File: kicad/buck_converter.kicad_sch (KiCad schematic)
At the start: 51 parts, among them J1 XT30U-M, J2 XT30U-F, Q1 BSZ146N10LS5ATMA1, Q2 BSZ146N10LS5ATMA1, U1 LM5146

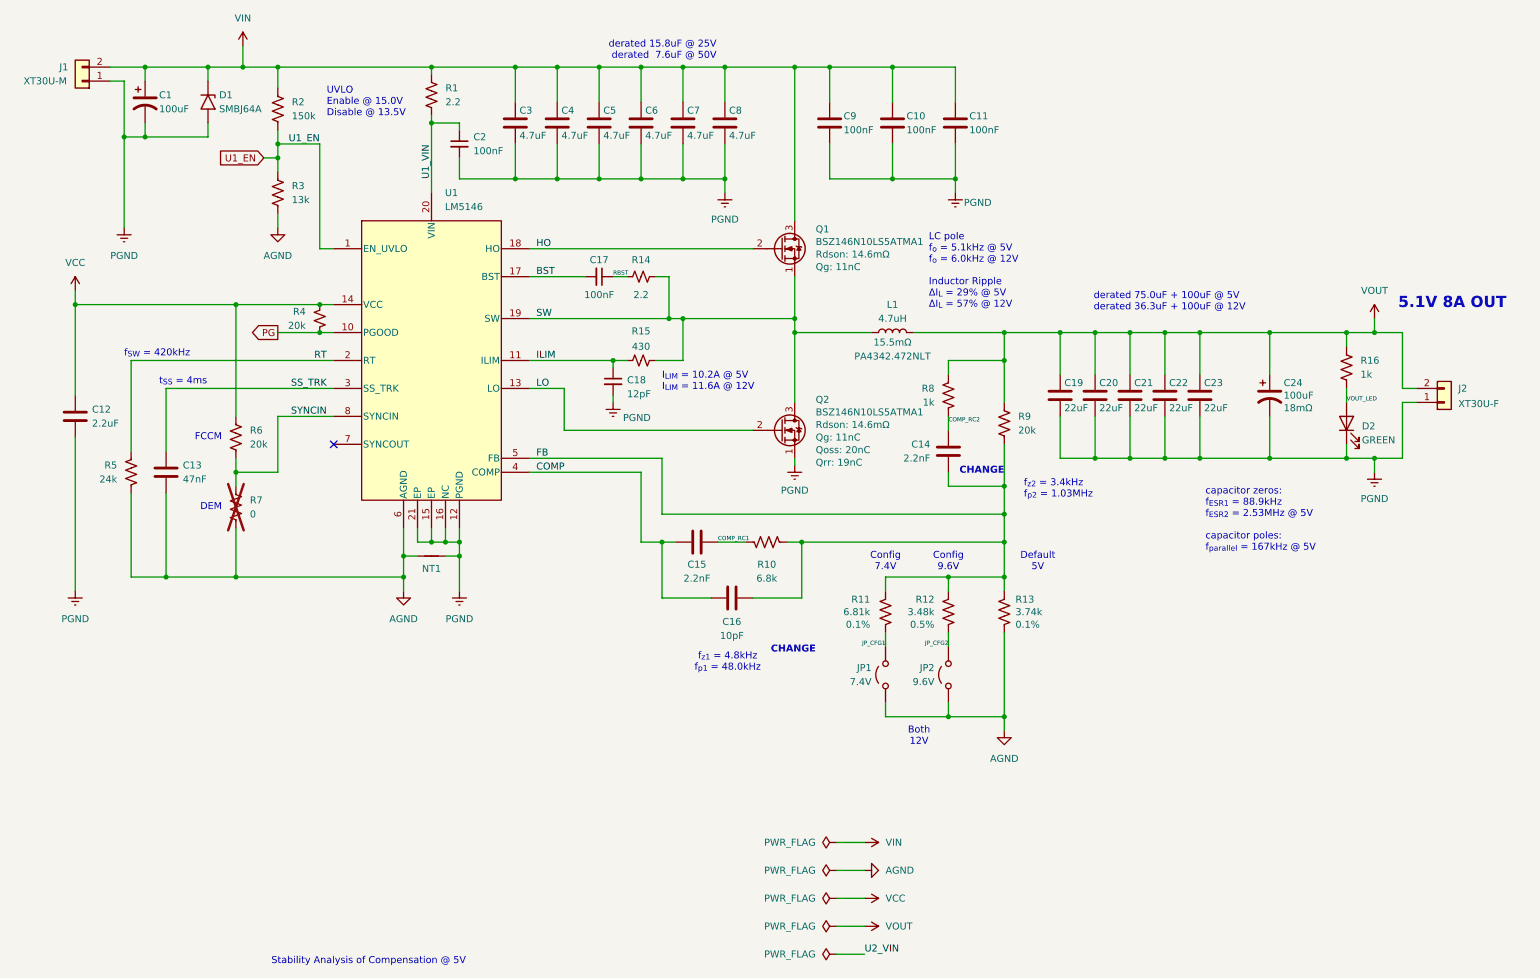
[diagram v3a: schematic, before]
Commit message: Wrong design files initially commited
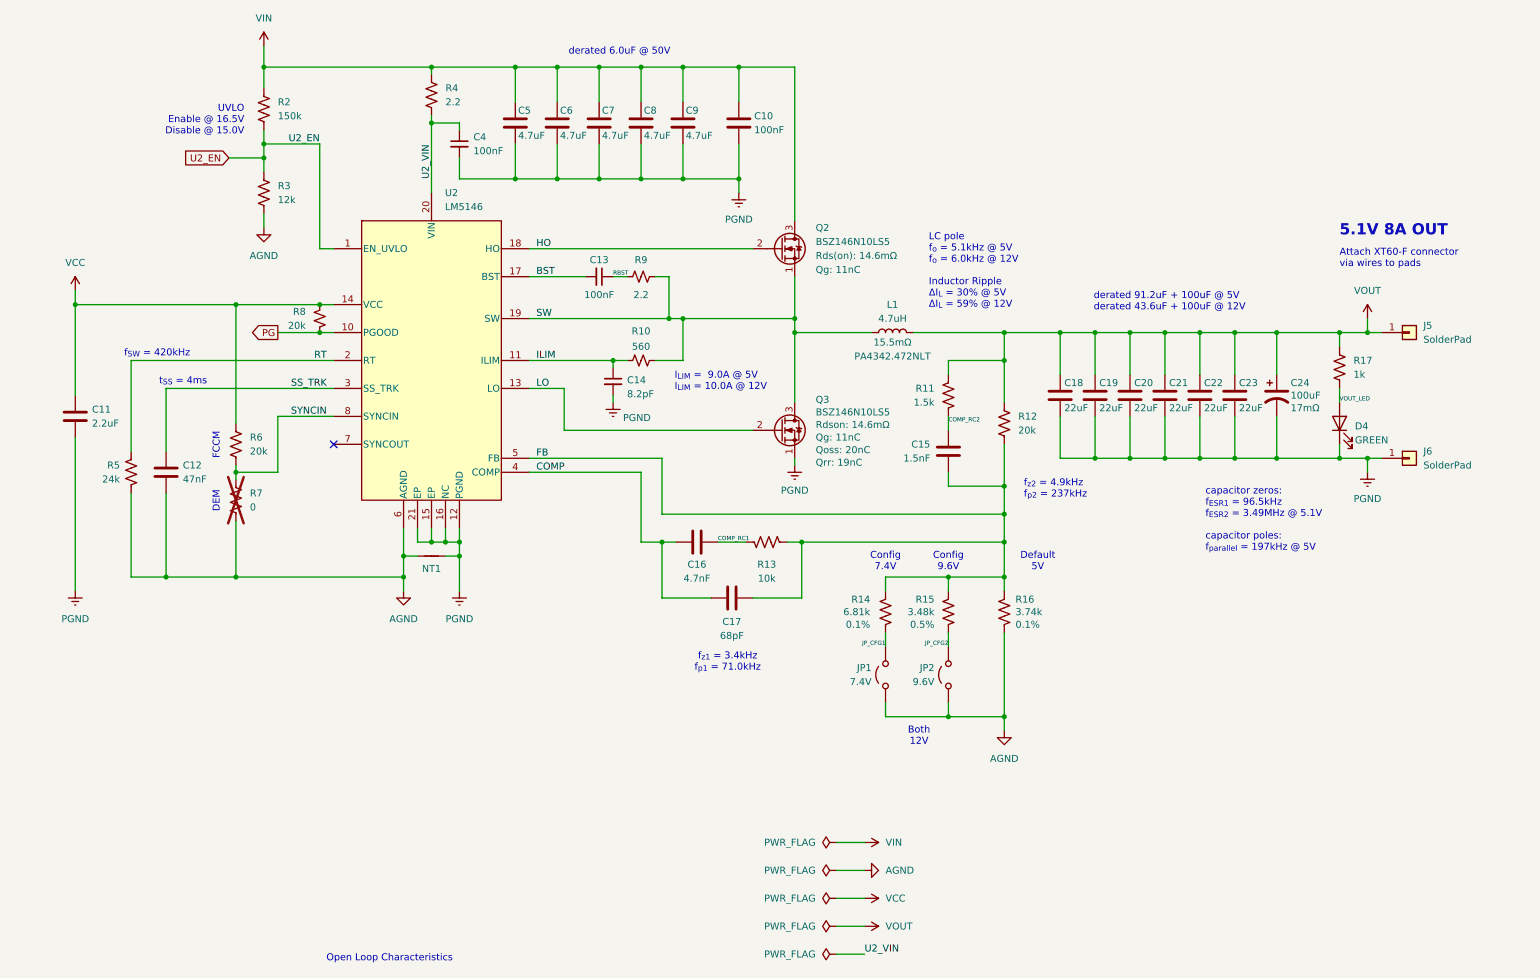
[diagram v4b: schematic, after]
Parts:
- removed C1: 100uF, Connector_Wire:SolderWire-0.5sqmm_1x02_P4.6mm_D0.9mm_OD2.1mm, symbol Device:C_Polarized_US
- removed C11: 100nF, Capacitor_SMD:C_0603_1608Metric, symbol Device:C
- removed C15: 2.2nF, Capacitor_SMD:C_0603_1608Metric, symbol Device:C
- removed C4, C6: 4.7uF, Capacitor_SMD:C_1206_3216Metric, symbol Device:C
- removed D1: SMBJ64A, Diode_SMD:D_SMB, symbol Diode:1.5SMCxxA
- removed J1: XT30U-M, Connector_AMASS:AMASS_XT30U-M_1x02_P5.0mm_Vertical, symbol Connector_Generic:Conn_01x02
- removed J2: XT30U-F, Connector_AMASS:AMASS_XT30U-F_1x02_P5.0mm_Vertical, symbol Connector_Generic:Conn_01x02
- removed Q1: BSZ146N10LS5ATMA1, Package_SON_JJ:Infineon_PG-TSDSON-8-26_3.3x3.3mm_P0.65mm_ThermalVias-D0.3mm, symbol Julian_Symbols:BSZ096N10LS5
- added C16: 4.7nF, Capacitor_SMD:C_0603_1608Metric, symbol Device:C
- added C22: 22uF, Capacitor_SMD:C_1206_3216Metric, symbol Device:C
- added J5, J6: SolderPad, Connector_Wire:SolderWirePad_1x01_SMD_3x6mm, symbol Connector_Generic:Conn_01x01
- added Q2: BSZ146N10LS5, Package_SON_JJ:Infineon_PG-TSDSON-8-26_3.3x3.3mm_P0.65mm_ThermalVias-D0.3mm, symbol Julian_Symbols:BSZ096N10LS5
- C14: renamed from C18; value 12pF -> 8.2pF; LCSC PN C576801 -> C2212506; Manufacturer YAGEO -> Murata Electronics; Part Number CC0603JRNPO0BN120 -> GCM1885C2A8R2DA16D
- C15: renamed from C14; value 2.2nF -> 1.5nF; LCSC PN C1604 -> C1595; Part Number 0603B222K500NT -> 0603B152K500NT; Part Type Basic -> Preferred Extended
- C17: renamed from C16; value 10pF -> 68pF; LCSC PN C1634 -> C28262; Part Number CL10C100JB8NNNC -> CL10C680JB8NNNC; Part Type Basic -> Preferred Extended
- C24: ESR 18mΩ -> 17mΩ; FT Rotation Offset 0 -> 180; LCSC PN C696814 -> C212710; Part Number T521D107M025ATE040 -> T521D107M025ATE060
- C9: value 100nF -> 4.7uF; footprint Capacitor_SMD:C_0603_1608Metric -> Capacitor_SMD:C_1206_3216Metric; ESR (none) -> 2mΩ; LCSC PN C113803 -> C3864744; Manufacturer YAGEO -> Murata Electronics; Part Number CC0603KRX7R0BB104 -> GRJ31CZ72A475KE01L
- L1: LCSC ALT1 (none) -> C2041319; PART ALT1 (none) -> SRP1038A-4R7M
- Q3: renamed from Q2; value BSZ146N10LS5ATMA1 -> BSZ146N10LS5; footprint Package_SON_JJ:Infineon_PG-TSDSON-8-26_3.3x3.3mm_P0.65mm -> Package_SON_JJ:Infineon_PG-TSDSON-8-26_3.3x3.3mm_P0.65mm_ThermalVias-D0.3mm; ESR 14.6mΩ -> 9.6mΩ; LCSC ALT1 (none) -> C534697; PART ALT1 (none) -> BSZ097N10NS5
- R10: renamed from R15; value 430 -> 560; LCSC PN C23170 -> C23204; Part Number 0603WAF4300T5E -> 0603WAF5600T5E; Part Type Preferred Extended -> Basic
- R11: renamed from R8; value 1k -> 1.5k; LCSC PN C21190 -> C22843; Part Number 0603WAF1001T5E -> 0603WAF1501T5E
- R13: renamed from R10; value 6.8k -> 10k; LCSC PN (none) -> C25804; Part Number (none) -> 0603WAF1002T5E
- R16: renamed from R13; LCSC PN C849741 -> C860375; Part Number RT0603BRE073K74L -> RT0603BRB073K74L
- R3: value 13k -> 12k; LCSC PN C22797 -> C22790; Part Number 0603WAF1302T5E -> 0603WAF1202T5E
- renumbered C12 to C11, C13 to C12, C17 to C13, C19 to C18, C20 to C19, C21 to C20, C22 to C21, C2 to C4, C3 to C6, D2 to D4, R9 to R12, R11 to R14, R12 to R15, R16 to R17, R1 to R4, R4 to R8, R14 to R9, U1 to U2
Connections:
- net U1_VIN is gone; now on net U2_VIN: C4.1, R4.2, U2.20 (VIN)
- net COMP: now also C16.1
- net COMP_RC1: now also C16.2
- net HO: now also Q2.2 (G)
- net PGND: now also C22.2, J6.1 (Pin_1)
- net SW: now also Q2.1 (S)
- net VIN: now also Q2.3 (D)
- net VOUT: now also C22.1, J5.1 (Pin_1)
- net U1_EN renamed U2_EN
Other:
- note added: "Attach XT60-F connector via wires to pads"
- note added: "I_{LIM} = 9.0A @ 5V I_{LIM} = 10.0A @ 12V"
- note added: "LC pole f_{o} = 5.1kHz @ 5V f_{o} = 6.0kHz @ 12V Inductor Ripple ΔI_{L} = 30% @ 5V ΔI_{L} = 59% @ 12V"
- note added: "Open Loop Characteristics"
- note added: "UVLO Enable @ 16.5V Disable @ 15.0V"
- note added: "capacitor zeros: f_{ESR1} = 96.5kHz f_{ESR2} = 3.49MHz @ 5.1V capacitor poles: f_{parallel} = 197kHz @ 5V"
- note added: "derated 6.0uF @ 50V"
- note added: "derated 91.2uF + 100uF @ 5V derated 43.6uF + 100uF @ 12V"
- note added: "f_{z1} = 3.4kHz f_{p1} = 71.0kHz"
- note added: "f_{z2} = 4.9kHz f_{p2} = 237kHz"
- note removed: "CHANGE"
- note removed: "I_{LIM} = 10.2A @ 5V I_{LIM} = 11.6A @ 12V"
- note removed: "LC pole f_{o} = 5.1kHz @ 5V f_{o} = 6.0kHz @ 12V Inductor Ripple ΔI_{L} = 29% @ 5V ΔI_{L} = 57% @ 12V"
- note removed: "Stability Analysis of Compensation @ 5V"
- note removed: "UVLO Enable @ 15.0V Disable @ 13.5V"
- note removed: "capacitor zeros: f_{ESR1} = 88.9kHz f_{ESR2} = 2.53MHz @ 5V capacitor poles: f_{parallel} = 167kHz @ 5V"
- note removed: "derated 15.8uF @ 25V derated 7.6uF @ 50V"
- note removed: "derated 75.0uF + 100uF @ 5V derated 36.3uF + 100uF @ 12V"
- note removed: "f_{z1} = 4.8kHz f_{p1} = 48.0kHz"
- note removed: "f_{z2} = 3.4kHz f_{p2} = 1.03MHz"
- moved on the sheet: C24, C6, D4, R17, R2, R3, R6, R7
